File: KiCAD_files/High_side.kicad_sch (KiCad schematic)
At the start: 27 parts, among them U204 MCP6486UT-E/LT, U601 AMC1311DWV, U602 ACS723LLCTR-20AB-T

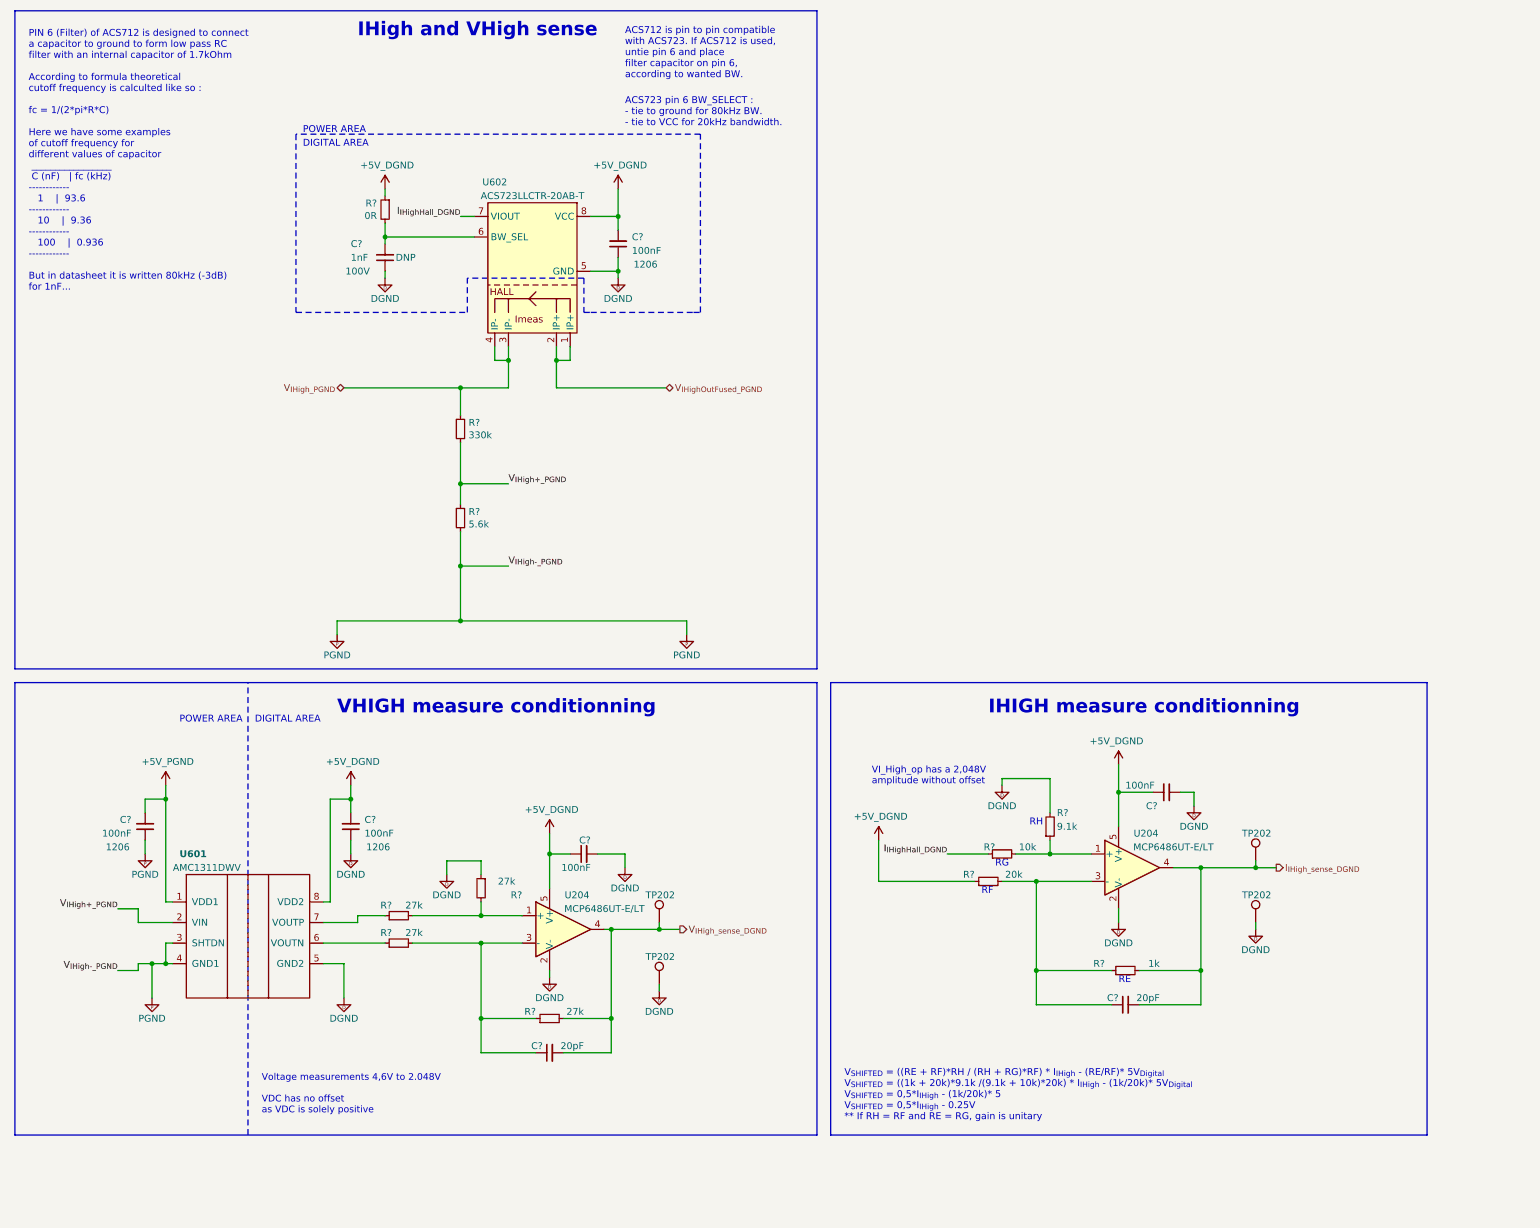
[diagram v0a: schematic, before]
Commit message: correct informations for capacitor: voltage, package, dielectric, correct informations for resistors: package, technology
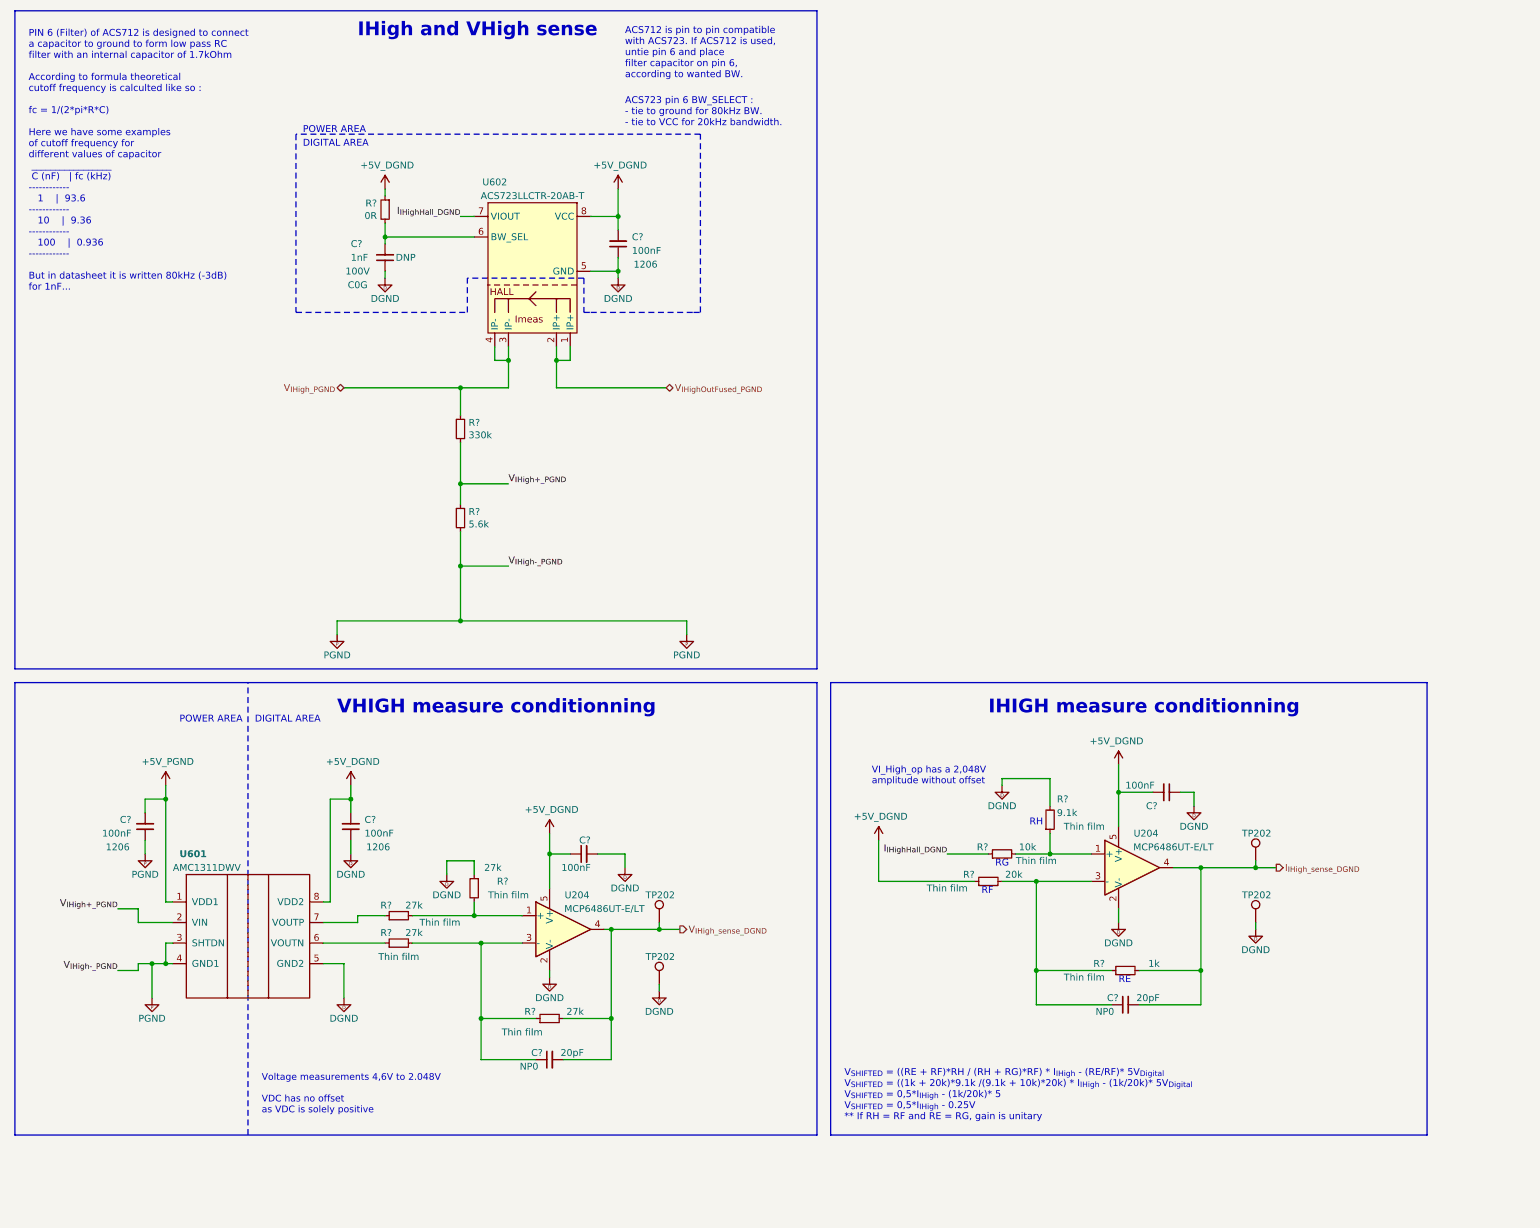
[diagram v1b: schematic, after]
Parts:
- C? (x2): Dielectric (none) -> NP0; Voltage (none) -> 50V
- C? (x5): Dielectric (none) -> X7R
- C?: Dielectric (none) -> C0G
- R? (x4): Technology (none) -> Thin film; manf# CR0805-FX-2702ELF -> RT0805FRE1327KL
- R? (x3): Technology (none) -> Thick film
- R?: Technology (none) -> Thin film; manf# CRT0805-FZ-1002ELF -> RT0805FRE1310KL
- R?: Technology (none) -> Thin film; manf# CR0805-FX-9101ELF -> RT0805FRE079K1L
- R?: Technology (none) -> Thin film; manf# CR0805-FX-2002ELF -> RT0805FRE1320KL
- R?: Technology (none) -> Thin film; manf# CR0805-FX-1001ELF -> RT0805FRE131KL
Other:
- moved on the sheet: C?, R?

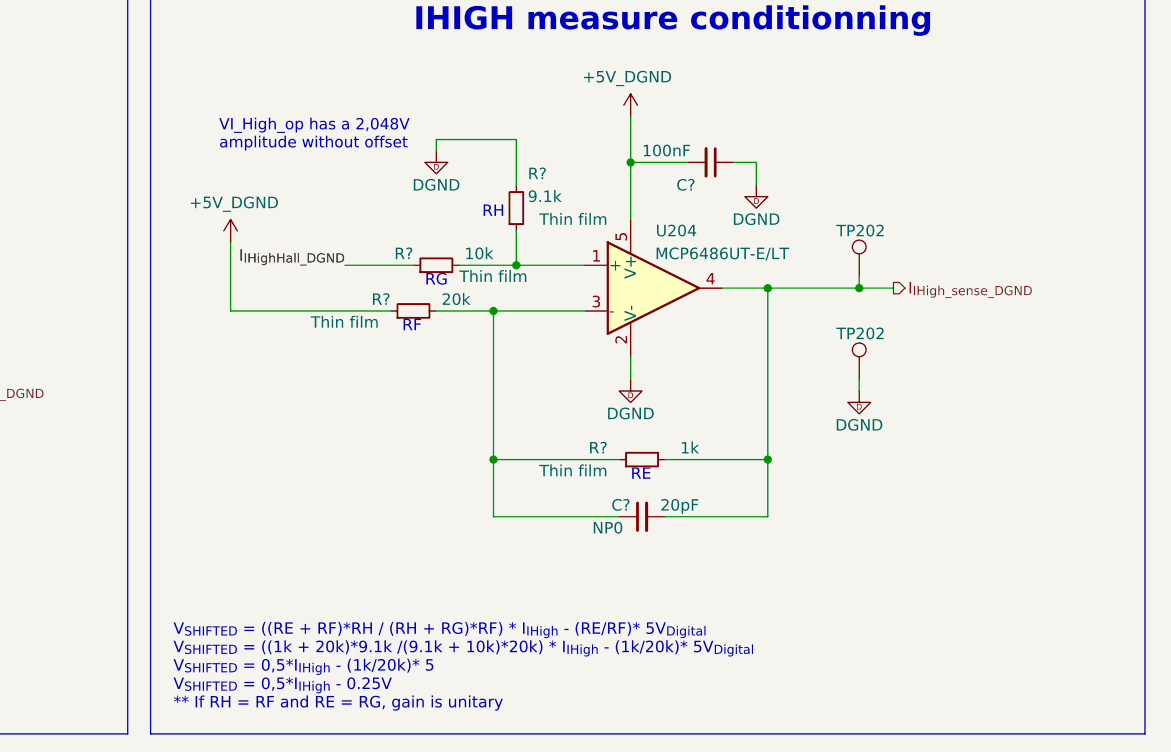
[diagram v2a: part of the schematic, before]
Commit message: corrected typo in ILow conditionning text" and corrected wrong resistor values for IHIGH conditionning: R609 is now 20k, R608 and R610 are now 5.9k
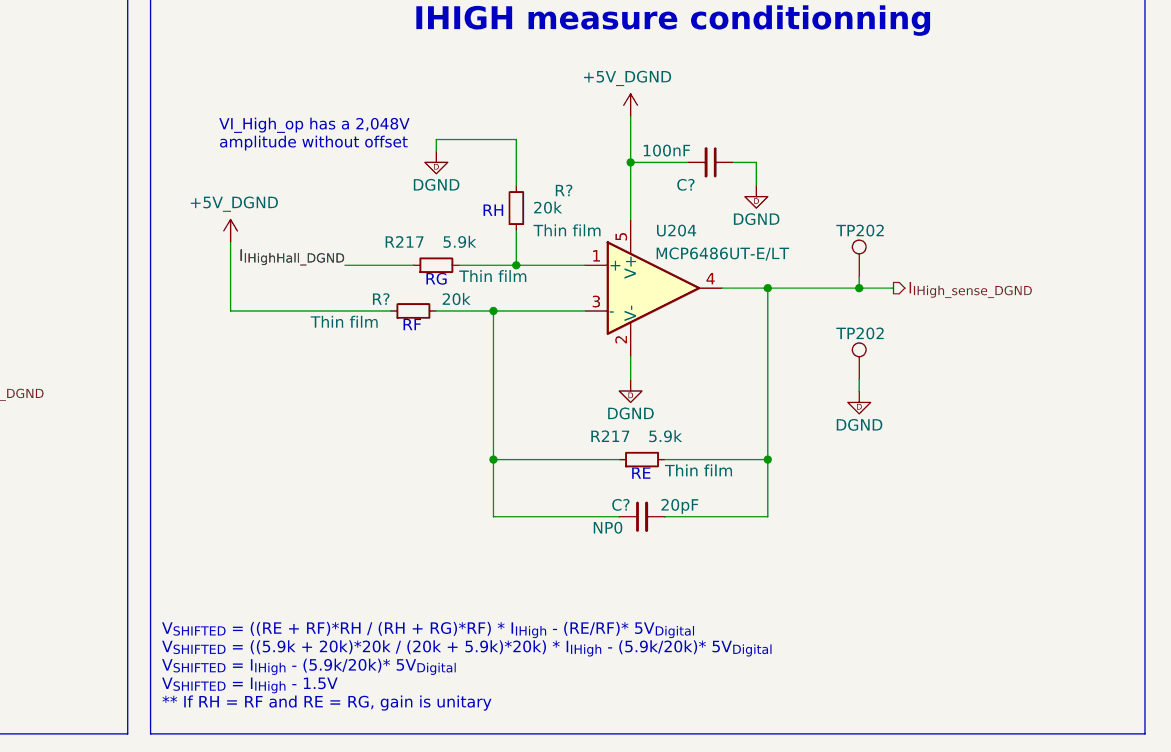
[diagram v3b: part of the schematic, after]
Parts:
- removed R?: 10k, Footprints:R_0805_2012Metric, symbol Device:R_Small
- removed R?: 9.1k, Footprints:R_0805_2012Metric, symbol Device:R_Small
- removed R?: 1k, Footprints:R_0805_2012Metric, symbol Device:R_Small
- added R217 (x2): 5.9k, Footprints:R_0805_2012Metric, symbol Device:R_Small
- added R?: 20k, Footprints:R_0805_2012Metric, symbol Device:R_Small
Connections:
- net DGND: now also R?.2
- net I_{IHighHall_DGND}: now also R217.1
- net I_{IHigh_sense_DGND}: now also R217.2
- net at C?.1, R?.2, U204.3 (-): now also R217.1
- net at U204.1 (+): now also R217.2, R?.1
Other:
- note added: "V_{SHIFTED} = ((RE + RF)*RH / (RH + RG)*RF) * I_{IHigh} - (RE/RF)* 5V_{Digital} V_{SHIFTED} = ((5.9k + 20k)*20k / (20k + 5.9k)*20k) * I_{IHigh} - (5.9k/20k)* 5V_{Digital} V_{SHIFTED} = I_{IHigh} - (5.9k/20k)* 5V_{Digital} V_{SHIFTED} = I_{IHigh} - 1.5V ** If RH = RF and RE = RG, gain is unitary"
- note removed: "V_{SHIFTED} = ((RE + RF)*RH / (RH + RG)*RF) * I_{IHigh} - (RE/RF)* 5V_{Digital} V_{SHIFTED} = ((1k + 20k)*9.1k /(9.1k + 10k)*20k) * I_{IHigh} - (1k/20k)* 5V_{Digital} V_{SHIFTED} = 0,5*I_{IHigh} - (1k/20k)* 5 V_{SHIFTED} = 0,5*I_{IHigh} - 0.25V ** If RH = RF and RE = RG, gain is unitary"

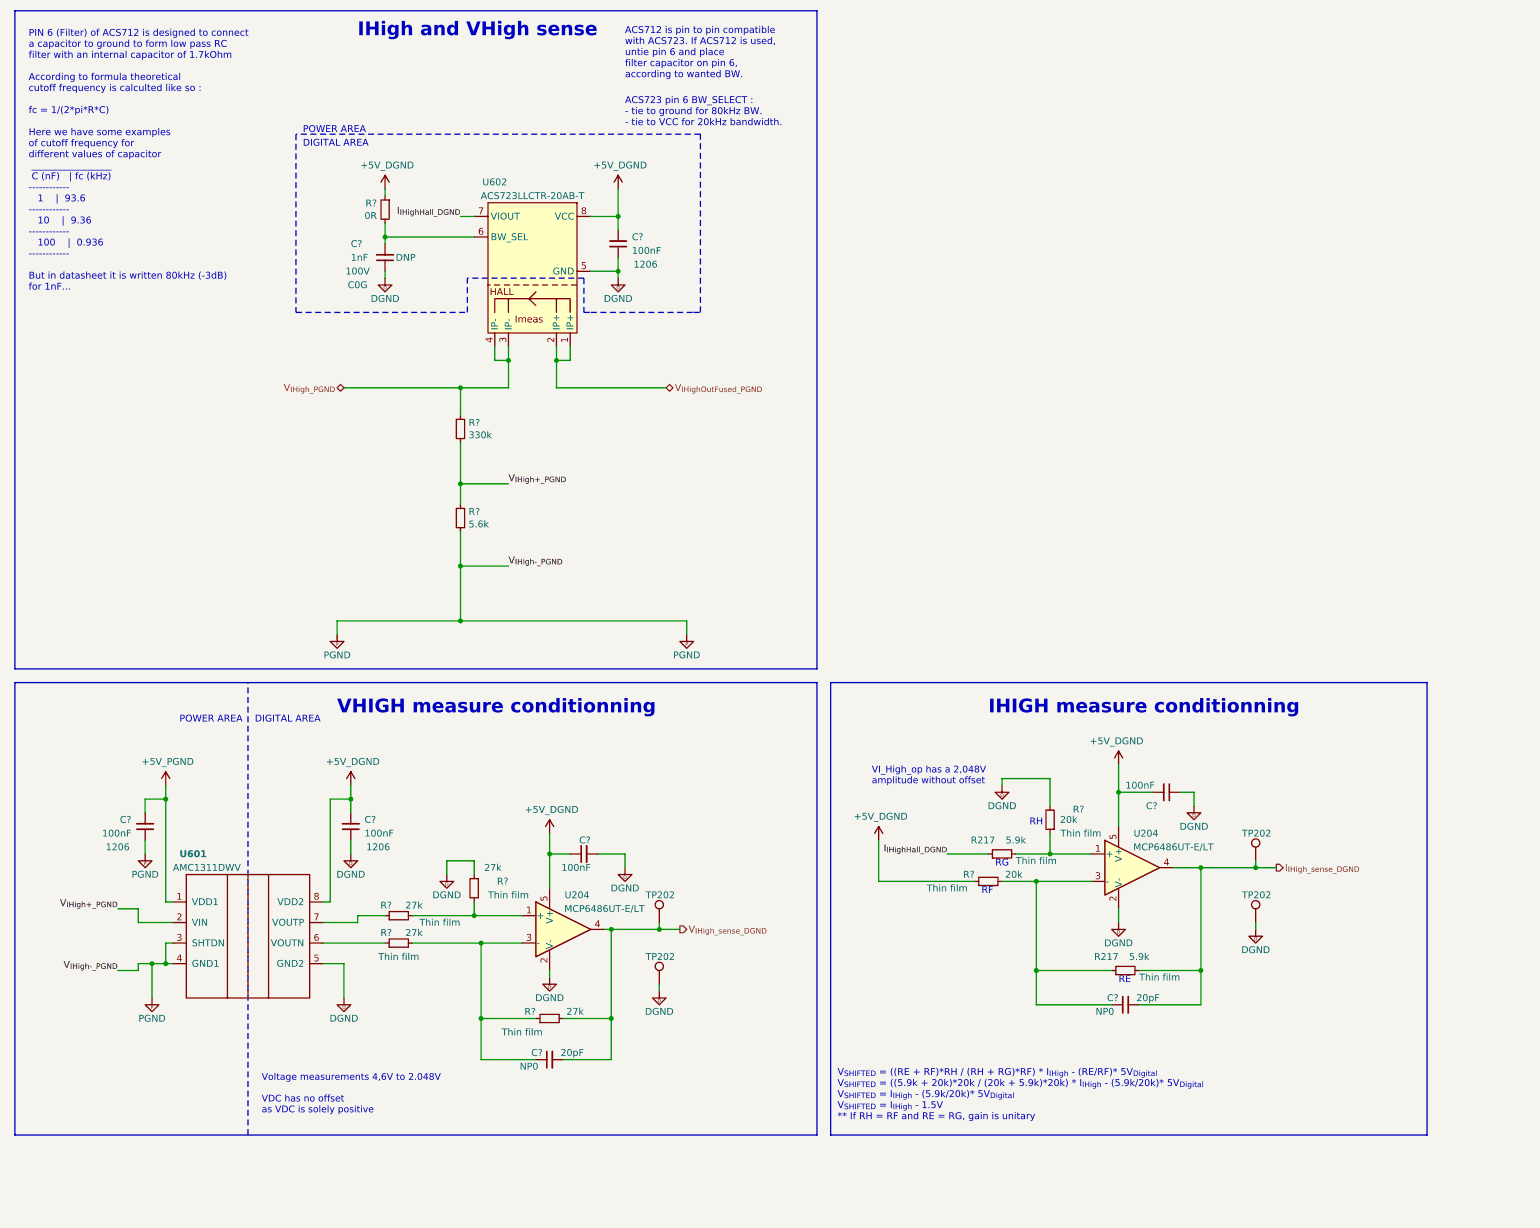
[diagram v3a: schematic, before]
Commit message: better comment on conditionning circuits (VHigh, VLow, Ihigh and ILOW)
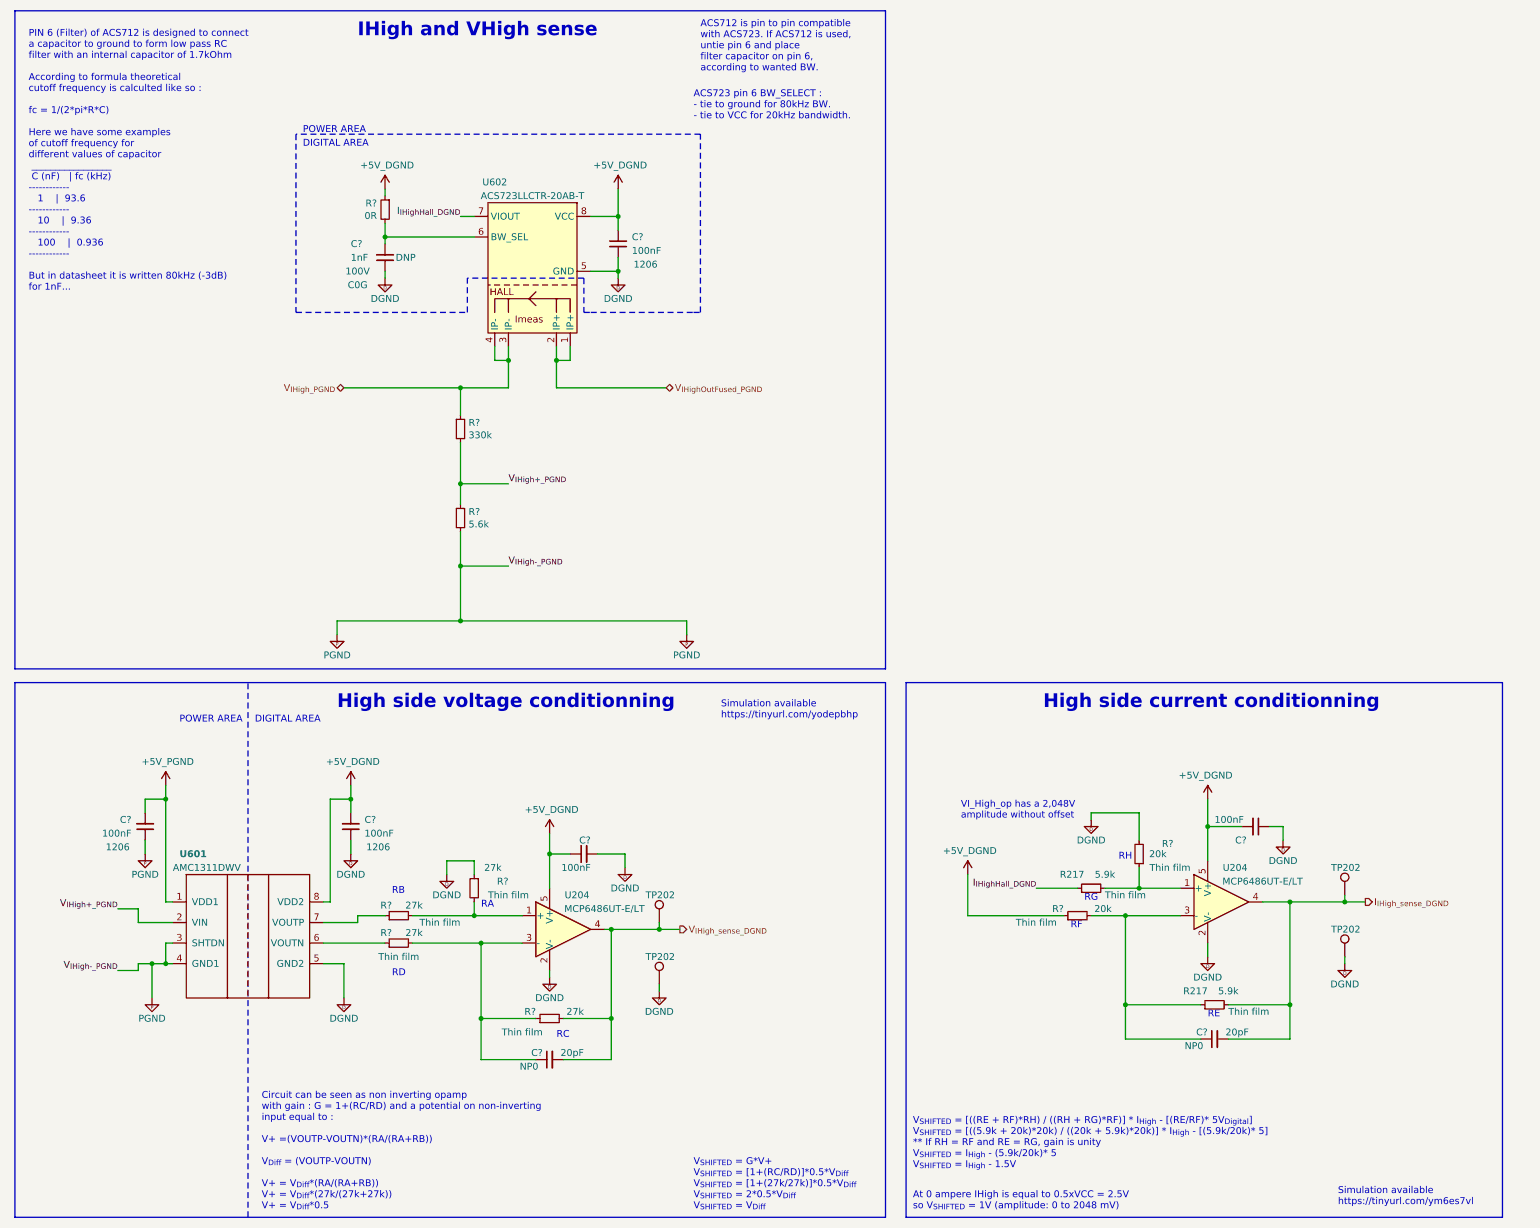
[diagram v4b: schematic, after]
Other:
- note added: "At 0 ampere IHigh is equal to 0.5xVCC = 2.5V so V_{SHIFTED} = 1V (amplitude: 0 to 2048 mV)"
- note added: "Circuit can be seen as non inverting opamp with gain : G = 1+(RC/RD) and a potential on non-inverting input equal to : V+ =(VOUTP-VOUTN)*(RA/(RA+RB)) V_{Diff} = (VOUTP-VOUTN) V+ = V_{Diff}*(RA/(RA+RB)) V+ = V_{Diff}*(27k/(27k+27k)) V+ = V_{Diff}*0.5"
- note added: "High side current conditionning"
- note added: "High side voltage conditionning"
- note added: "RA"
- note added: "RB"
- note added: "RC"
- note added: "RD"
- note added: "Simulation available https://tinyurl.com/ym6es7vl"
- note added: "Simulation available https://tinyurl.com/yodepbhp"
- note added: "V_{SHIFTED} = G*V+ V_{SHIFTED} = [1+(RC/RD)]*0.5*V_{Diff} V_{SHIFTED} = [1+(27k/27k)]*0.5*V_{Diff} V_{SHIFTED} = 2*0.5*V_{Diff} V_{SHIFTED} = V_{Diff}"
- note added: "V_{SHIFTED} = [((RE + RF)*RH) / ((RH + RG)*RF)] * I_{High} - [(RE/RF)* 5V_{Digital}] V_{SHIFTED} = [((5.9k + 20k)*20k) / ((20k + 5.9k)*20k)] * I_{High} - [(5.9k/20k)* 5] ** If RH = RF and RE = RG, gain is unity V_{SHIFTED} = I_{High} - (5.9k/20k)* 5 V_{SHIFTED} = I_{High} - 1.5V"
- note removed: "IHIGH measure conditionning"
- note removed: "VHIGH measure conditionning"
- note removed: "V_{SHIFTED} = ((RE + RF)*RH / (RH + RG)*RF) * I_{IHigh} - (RE/RF)* 5V_{Digital} V_{SHIFTED} = ((5.9k + 20k)*20k / (20k + 5.9k)*20k) * I_{IHigh} - (5.9k/20k)* 5V_{Digital} V_{SHIFTED} = I_{IHigh} - (5.9k/20k)* 5V_{Digital} V_{SHIFTED} = I_{IHigh} - 1.5V ** If RH = RF and RE = RG, gain is unitary"
- note removed: "Voltage measurements 4,6V to 2.048V VDC has no offset as VDC is solely positive"
- moved on the sheet: C?, R217, R?, TP202, U204
